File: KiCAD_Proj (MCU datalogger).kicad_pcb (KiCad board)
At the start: 2 copper layers, 52.3 x 34.7 mm, 31 parts, among them J1 Conn_01x04_Pin, J2 Conn_01x09_Pin, J3 Conn_01x04_Pin, J4 Conn_02x03_Counter_Clockwise, U1 24LC1025-I_SM, U2 DS1337S_, U3 24LC1025-I_SM, U4 ATMEGA328P-AU, Y1 32.768 KHz, Y2 16MHz

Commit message: Updated the pcb.
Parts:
- moved C3 11.6 mm to (110.9, 90.0)
- moved C5 11.6 mm to (116.0, 90.0)
- moved D1 11.6 mm to (125.5, 90.0)
- moved D2 11.6 mm to (121.1, 90.0)
- moved G*** 11.6 mm to (98.5, 98.9)
- moved J3 11.6 mm to (119.8, 114.8)
- moved R5 11.6 mm to (125.5, 93.8)
- moved R7 11.6 mm to (121.1, 93.8)
- moved C1 11.6 mm to (106.5, 90.0)
- moved J2 11.6 mm to (94.4, 114.8)
- moved U1 11.6 mm to (98.8, 98.9)
- moved U2 11.6 mm to (98.8, 105.9)
- moved U3 11.6 mm to (98.8, 91.9)
- moved BT1 11.6 mm to (90.8, 96.4)
- moved C2 11.6 mm to (121.1, 105.2)
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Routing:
- net /Vcc: track 178.4 -> 43.8 mm, vias 10 -> 13
- net GND: track 84.2 -> 43.6 mm, vias 12 -> 11
- net /SCK: track 97.6 -> 86.6 mm, vias 3 -> 5
- net /D8: track 12.0 -> 20.4 mm, vias 1 -> 0
- net /RX: track 27.6 -> 33.0 mm, vias 1 -> 0
- net /TX: track 32.1 -> 36.5 mm, vias 1 -> 0
- net Net-(U4-PB7): track 28.4 -> 25.2 mm, vias 2 -> 3
- net Net-(U2-~{INTA}): track 8.02 -> 5.12 mm
- net /SDA: track 57.4 -> 55.1 mm, vias 2 -> 5
- net /MOSI: track 24.7 -> 26.6 mm, vias 0 -> 2
- net /D5: track 14.3 -> 15.8 mm, vias 1 -> 0
- net Net-(U4-AREF): track 18.0 -> 19.4 mm
- net /D2: track 29.8 -> 31.1 mm, vias 1 -> 0
- net /D7: track 16.2 -> 15.2 mm, vias 1 -> 0
- net Net-(U4-PB6): track 25.5 -> 24.6 mm, vias 0 -> 3
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- added copper zone on In1.Cu, net /Vcc
- removed copper zone on F.Cu, net /Vcc
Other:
- copper layers 2 -> 4

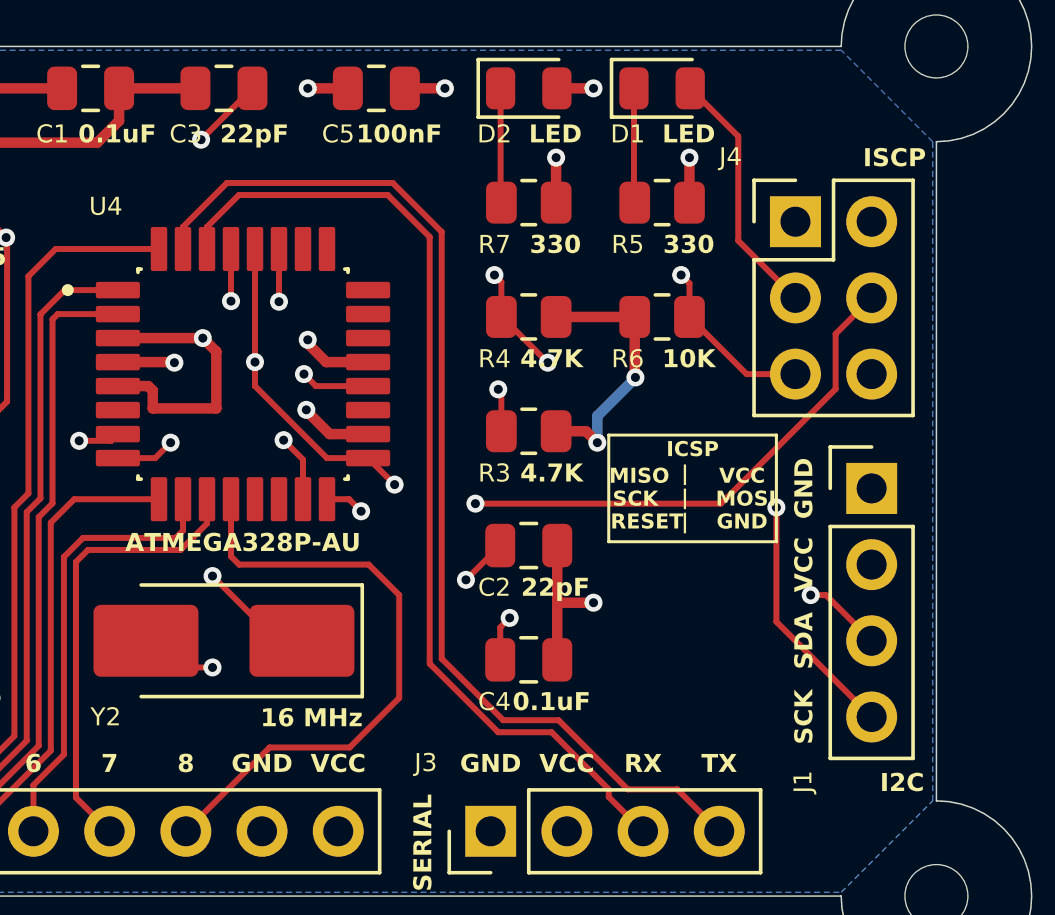
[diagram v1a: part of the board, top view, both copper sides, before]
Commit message: Fixed the wirings on the PCB.
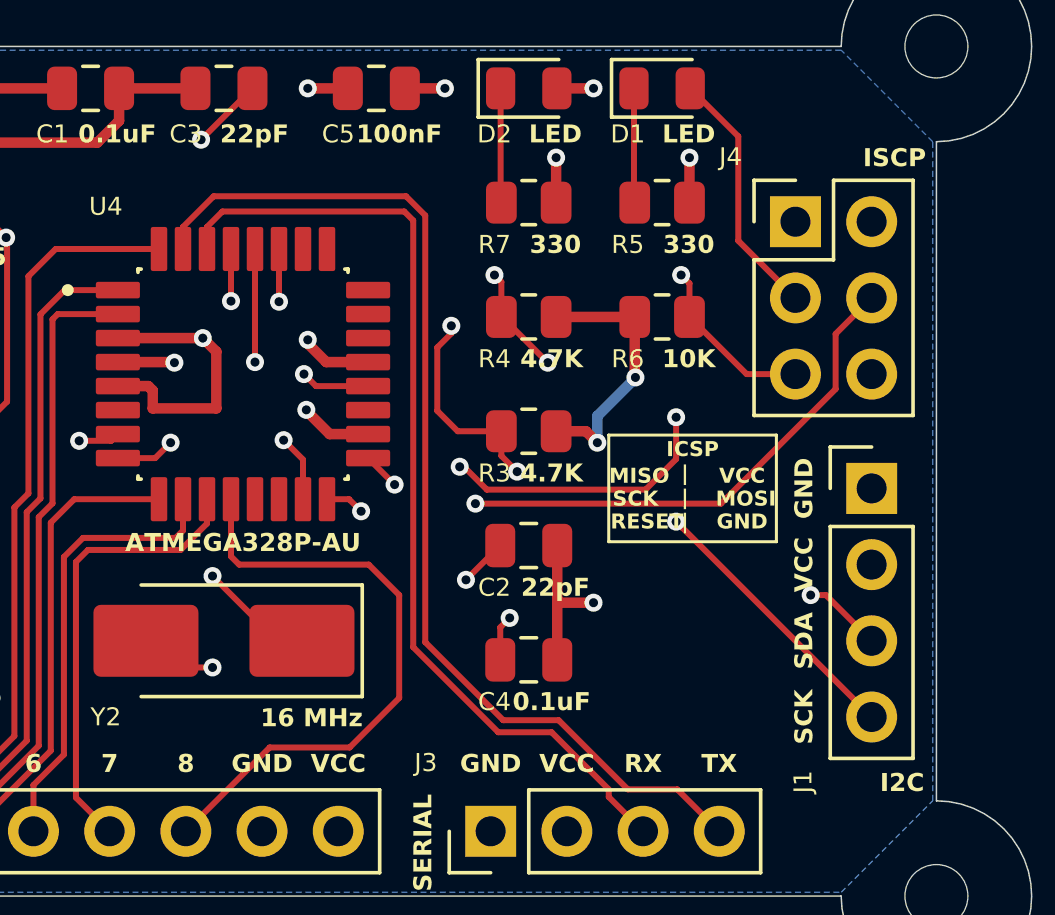
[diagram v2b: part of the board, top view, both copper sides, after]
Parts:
- moved REF** 0.68 mm to (98.8, 92.8)
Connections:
- J1 pad 4: /SCK -> /SCL
- R3 pad 2: /SCK -> /SCL
- U1 pad 6: /SCK -> /SCL
- U2 pad 6: /SCK -> /SCL
- U3 pad 6: /SCK -> /SCL
- U4 pad 28: /SCK -> /SCL
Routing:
- net /SCL: track 0.00 -> 67.7 mm, vias 0 -> 5
- net /SCK: track 86.6 -> 27.5 mm, vias 5 -> 3

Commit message: Change the title.
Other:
- board text removed: "ICSP"
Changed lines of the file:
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@@
 		)
 	)
-	(gr_text "ICSP"
+	(gr_text "ISCP"
 		(at 126.532936 102.321064 0)
 		(layer "F.SilkS")
@@
 		(min_thickness 0.254)
 		(filled_areas_thickness no)
-		(fill yes
+		(fill
 			(mode hatch)
 			(thermal_gap 0.508)
@@
 		(min_thickness 0.254)
 		(filled_areas_thickness no)
-		(fill yes
+		(fill
 			(mode hatch)
 			(thermal_gap 0.508)
